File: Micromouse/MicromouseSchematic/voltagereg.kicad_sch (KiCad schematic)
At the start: 5 parts

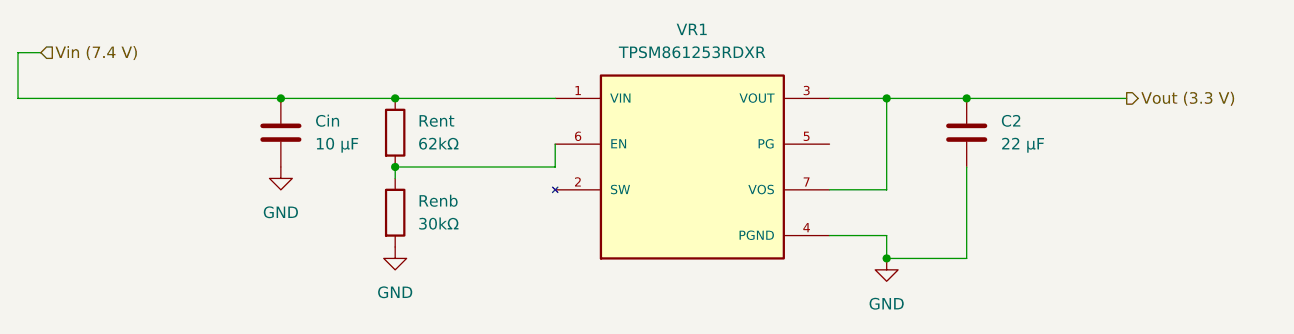
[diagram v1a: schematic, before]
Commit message: changed motor driver schematics
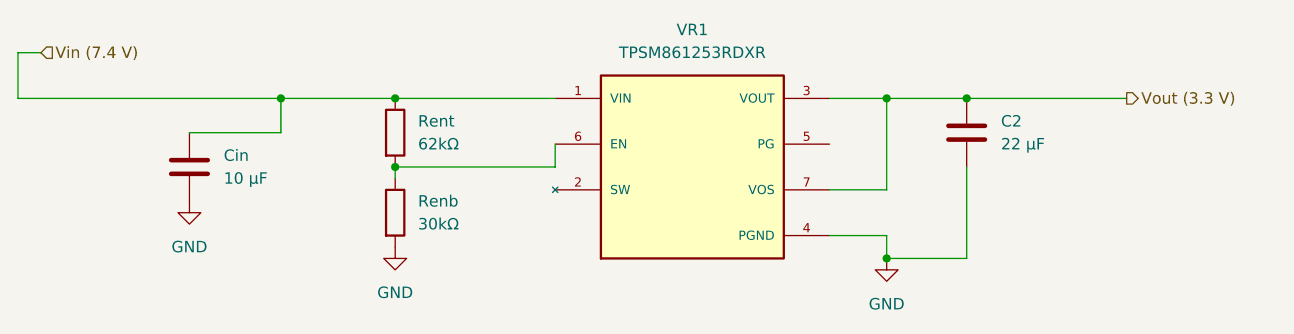
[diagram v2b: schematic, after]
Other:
- moved on the sheet: Cin
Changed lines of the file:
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@@
 	(paper "A4")
 	(junction
+		(at 161.29 107.95)
+		(diameter 0)
+		(color 0 0 0 0)
+	)
+	(junction
 		(at 93.98 90.17)
 		(diameter 0)
@@
 	)
 	(junction
-		(at 161.29 107.95)
-		(diameter 0)
-		(color 0 0 0 0)
-	)
-	(junction
 		(at 106.68 97.79)
 		(diameter 0)
@@
 	(wire
 		(pts
+			(xy 83.82 93.98) (xy 93.98 93.98)
+		)
+		(stroke
+			(width 0)
+			(type default)
+		)
+	)
+	(wire
+		(pts
 			(xy 154.94 100.33) (xy 161.29 100.33)
 		)
@@
 	(wire
 		(pts
+			(xy 93.98 93.98) (xy 93.98 90.17)
+		)
+		(stroke
+			(width 0)
+			(type default)
+		)
+	)
+	(wire
+		(pts
 			(xy 106.68 97.79) (xy 106.68 99.06)
 		)
@@
 	(wire
 		(pts
+			(xy 124.46 97.79) (xy 106.68 97.79)
+		)
+		(stroke
+			(width 0)
+			(type default)
+		)
+	)
+	(wire
+		(pts
+			(xy 64.77 90.17) (xy 93.98 90.17)
+		)
+		(stroke
+			(width 0)
+			(type default)
+		)
+	)
+	(wire
+		(pts
+			(xy 170.18 107.95) (xy 161.29 107.95)
+		)
+		(stroke
+			(width 0)
+			(type default)
+		)
+	)
+	(wire
+		(pts
+			(xy 154.94 90.17) (xy 161.29 90.17)
+		)
+		(stroke
+			(width 0)
+			(type default)
+		)
+	)
+	(wire
+		(pts
+			(xy 161.29 100.33) (xy 161.29 90.17)
+		)
+		(stroke
+			(width 0)
+			(type default)
+		)
+	)
+	(wire
+		(pts
+			(xy 161.29 105.41) (xy 161.29 107.95)
+		)
+		(stroke
+			(width 0)
+			(type default)
+		)
+	)
+	(wire
+		(pts
 			(xy 93.98 90.17) (xy 106.68 90.17)
-		)
-		(stroke
-			(width 0)
-			(type default)
-		)
-	)
-	(wire
-		(pts
-			(xy 124.46 97.79) (xy 106.68 97.79)
-		)
-		(stroke
-			(width 0)
-			(type default)
-		)
-	)
-	(wire
-		(pts
-			(xy 93.98 90.17) (xy 64.77 90.17)
-		)
-		(stroke
-			(width 0)
-			(type default)
-		)
-	)
-	(wire
-		(pts
-			(xy 170.18 107.95) (xy 161.29 107.95)
-		)
-		(stroke
-			(width 0)
-			(type default)
-		)
-	)
-	(wire
-		(pts
-			(xy 154.94 90.17) (xy 161.29 90.17)
-		)
-		(stroke
-			(width 0)
-			(type default)
-		)
-	)
-	(wire
-		(pts
-			(xy 161.29 100.33) (xy 161.29 90.17)
-		)
-		(stroke
-			(width 0)
-			(type default)
-		)
-	)
-	(wire
-		(pts
-			(xy 161.29 105.41) (xy 161.29 107.95)
 		)
 		(stroke
@@
 	(symbol
 		(lib_id "power:GND")
-		(at 93.98 97.79 0)
+		(at 83.82 101.6 0)
 		(unit 1)
 		(exclude_from_sim no)
@@
 		(fields_autoplaced yes)
 		(property "Reference" "#PWR04"
-			(at 93.98 104.14 0)
+			(at 83.82 107.95 0)
 			(effects
 				(font
@@
 		)
 		(property "Value" "GND"
-			(at 93.98 102.87 0)
+			(at 83.82 106.68 0)
 			(effects
 				(font
@@
 		)
 		(property "Footprint" ""
-			(at 93.98 97.79 0)
+			(at 83.82 101.6 0)
 			(effects
 				(font
@@
 		)
 		(property "Datasheet" ""
-			(at 93.98 97.79 0)
+			(at 83.82 101.6 0)
 			(effects
 				(font
@@
 		)
 		(property "Description" "Power symbol creates a global label with name \"GND\" , ground"
-			(at 93.98 97.79 0)
+			(at 83.82 101.6 0)
 			(effects
 				(font
@@
 	(symbol
 		(lib_id "Device:C")
-		(at 93.98 93.98 0)
+		(at 83.82 97.79 0)
 		(unit 1)
 		(exclude_from_sim no)
@@
 		(fields_autoplaced yes)
 		(property "Reference" "Cin"
-			(at 97.79 92.7099 0)
+			(at 87.63 96.5199 0)
 			(effects
 				(font
@@
 		)
 		(property "Value" "10 µF"
-			(at 97.79 95.2499 0)
+			(at 87.63 99.0599 0)
 			(effects
 				(font
@@
 		)
 		(property "Footprint" ""
-			(at 94.9452 97.79 0)
+			(at 84.7852 101.6 0)
 			(effects
 				(font
@@
 		)
 		(property "Datasheet" "~"
-			(at 93.98 93.98 0)
+			(at 83.82 97.79 0)
 			(effects
 				(font
@@
 		)
 		(property "Description" "Unpolarized capacitor"
-			(at 93.98 93.98 0)
-			(effects
-				(font
+			(at 83.82 97.79 0)
+			(effects
+				(font

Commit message: Added IR, programming header, i2c & timer pins
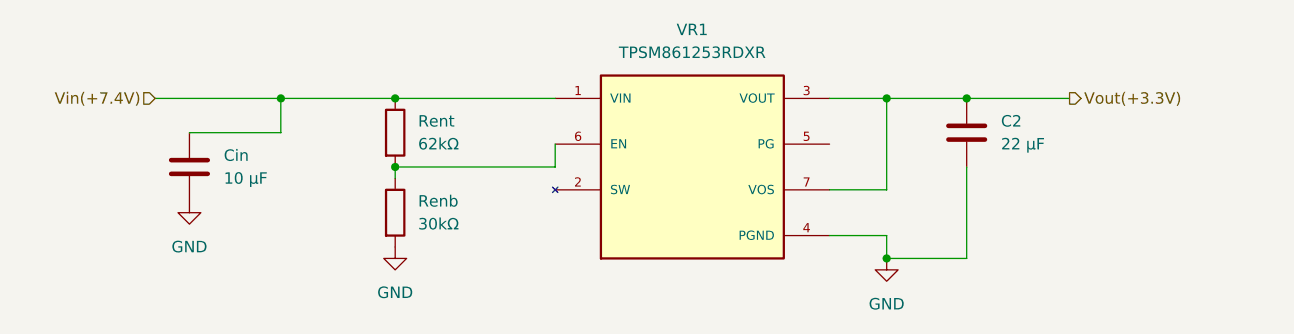
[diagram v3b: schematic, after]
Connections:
- net Vin (7.4 V) renamed Vin(+7.4V)
- net Vout (3.3 V) renamed Vout(+3.3V)
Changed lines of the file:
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@@
 	(wire
 		(pts
-			(xy 64.77 85.09) (xy 67.31 85.09)
+			(xy 80.01 90.17) (xy 93.98 90.17)
 		)
 		(stroke
@@
 	(wire
 		(pts
-			(xy 170.18 90.17) (xy 187.96 90.17)
+			(xy 170.18 90.17) (xy 181.61 90.17)
 		)
 		(stroke
@@
 		(pts
 			(xy 154.94 100.33) (xy 161.29 100.33)
-		)
-		(stroke
-			(width 0)
-			(type default)
-		)
-	)
-	(wire
-		(pts
-			(xy 64.77 90.17) (xy 64.77 85.09)
 		)
 		(stroke
@@
 		(pts
 			(xy 124.46 97.79) (xy 106.68 97.79)
-		)
-		(stroke
-			(width 0)
-			(type default)
-		)
-	)
-	(wire
-		(pts
-			(xy 64.77 90.17) (xy 93.98 90.17)
 		)
 		(stroke
@@
 		)
 	)
-	(hierarchical_label "Vin (7.4 V)"
+	(hierarchical_label "Vin(+7.4V)"
 		(shape input)
-		(at 67.31 85.09 0)
+		(at 80.01 90.17 180)
 		(effects
 			(font
 				(size 1.27 1.27)
 			)
-			(justify left)
+			(justify right)
 		)
 	)
-	(hierarchical_label "Vout (3.3 V)"
+	(hierarchical_label "Vout(+3.3V)"
 		(shape output)
-		(at 187.96 90.17 0)
+		(at 181.61 90.17 0)
 		(effects
 			(font

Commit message: added some stuff
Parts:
- VR1: footprint TPSM861253RDXR:VREG_TPSM861253RDXR -> TPSM862253RDXR_FOOTPRINT:TPSM861253RDXR
- renumbered Cin to Cin_VR1, Renb to Renb1, Rent to Rent1
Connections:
- no-connect marks 0 -> 1
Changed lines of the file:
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@@
 		(color 0 0 0 0)
+	)
+	(no_connect
+		(at 154.94 95.25)
 	)
 	(wire
@@
 		(dnp no)
 		(fields_autoplaced yes)
-		(property "Reference" "Cin"
+		(property "Reference" "Cin_VR1"
 			(at 87.63 96.5199 0)
 			(effects
@@
 			(project "MicromouseSchematic"
 				(path "/0dcfab91-6b00-43c0-ac0b-8c301cb559e5/3cd5e638-0450-45f9-91e1-d72f396e0d78"
-					(reference "Cin")
+					(reference "Cin_VR1")
 					(unit 1)
 				)
@@
 			)
 		)
-		(property "Footprint" "TPSM861253RDXR:VREG_TPSM861253RDXR"
+		(property "Footprint" "TPSM862253RDXR_FOOTPRINT:TPSM861253RDXR"
 			(at 139.7 97.79 0)
 			(effects
@@
 		(dnp no)
 		(fields_autoplaced yes)
-		(property "Reference" "Rent"
+		(property "Reference" "Rent1"
 			(at 109.22 92.7099 0)
 			(effects
@@
 			(project "MicromouseSchematic"
 				(path "/0dcfab91-6b00-43c0-ac0b-8c301cb559e5/3cd5e638-0450-45f9-91e1-d72f396e0d78"
-					(reference "Rent")
+					(reference "Rent1")
 					(unit 1)
 				)
@@
 		(dnp no)
 		(fields_autoplaced yes)
-		(property "Reference" "Renb"
+		(property "Reference" "Renb1"
 			(at 109.22 101.5999 0)
 			(effects
@@
 			(project "MicromouseSchematic"
 				(path "/0dcfab91-6b00-43c0-ac0b-8c301cb559e5/3cd5e638-0450-45f9-91e1-d72f396e0d78"
-					(reference "Renb")
+					(reference "Renb1")
 					(unit 1)
 				)

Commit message: Micromouse KiCad: MP6550 libs in project, fp-lib paths, schematic updates
Move MP6550G-Z symbol and legacy footprints into MicromouseSchematic, add
MP6550G-Z.pretty with MP6550_MNP footprint, and point fp-lib-table at the
project-local MM_MP6550G-Z library.

Replace old absolute footprint paths with this repo’s Micromouse tree and
MM_* library names. Update root schematic and IMU/IR/motor/TOF/regulator
subsheets; add empty bluethooth.kicad_sch hierarchical sheet. Extend KiCad
project BOM field configuration; refresh fp-info-cache. Drop schematic lock
file; include dated schematic backup zip.
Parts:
- VR1: footprint TPSM862253RDXR_FOOTPRINT:TPSM861253RDXR -> MM_TPSM861253RDXR:TPSM861253RDXR
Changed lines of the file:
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@@
 			)
 		)
-		(property "Footprint" "TPSM862253RDXR_FOOTPRINT:TPSM861253RDXR"
+		(property "Footprint" "MM_TPSM861253RDXR:TPSM861253RDXR"
 			(at 139.7 97.79 0)
 			(effects

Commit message: assigned capacitor footprints. still have to figure out rest
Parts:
- C2: footprint (none) -> Capacitor_SMD:C_0603_1608Metric
- Cin_VR1: footprint (none) -> Capacitor_SMD:C_0805_2012Metric
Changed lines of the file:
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@@
 			)
 		)
-		(property "Footprint" ""
+		(property "Footprint" "Capacitor_SMD:C_0603_1608Metric"
 			(at 171.1452 97.79 0)
 			(effects
@@
 			)
 		)
-		(property "Footprint" ""
+		(property "Footprint" "Capacitor_SMD:C_0805_2012Metric"
 			(at 84.7852 101.6 0)
 			(effects
